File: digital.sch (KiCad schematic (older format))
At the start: 2 parts

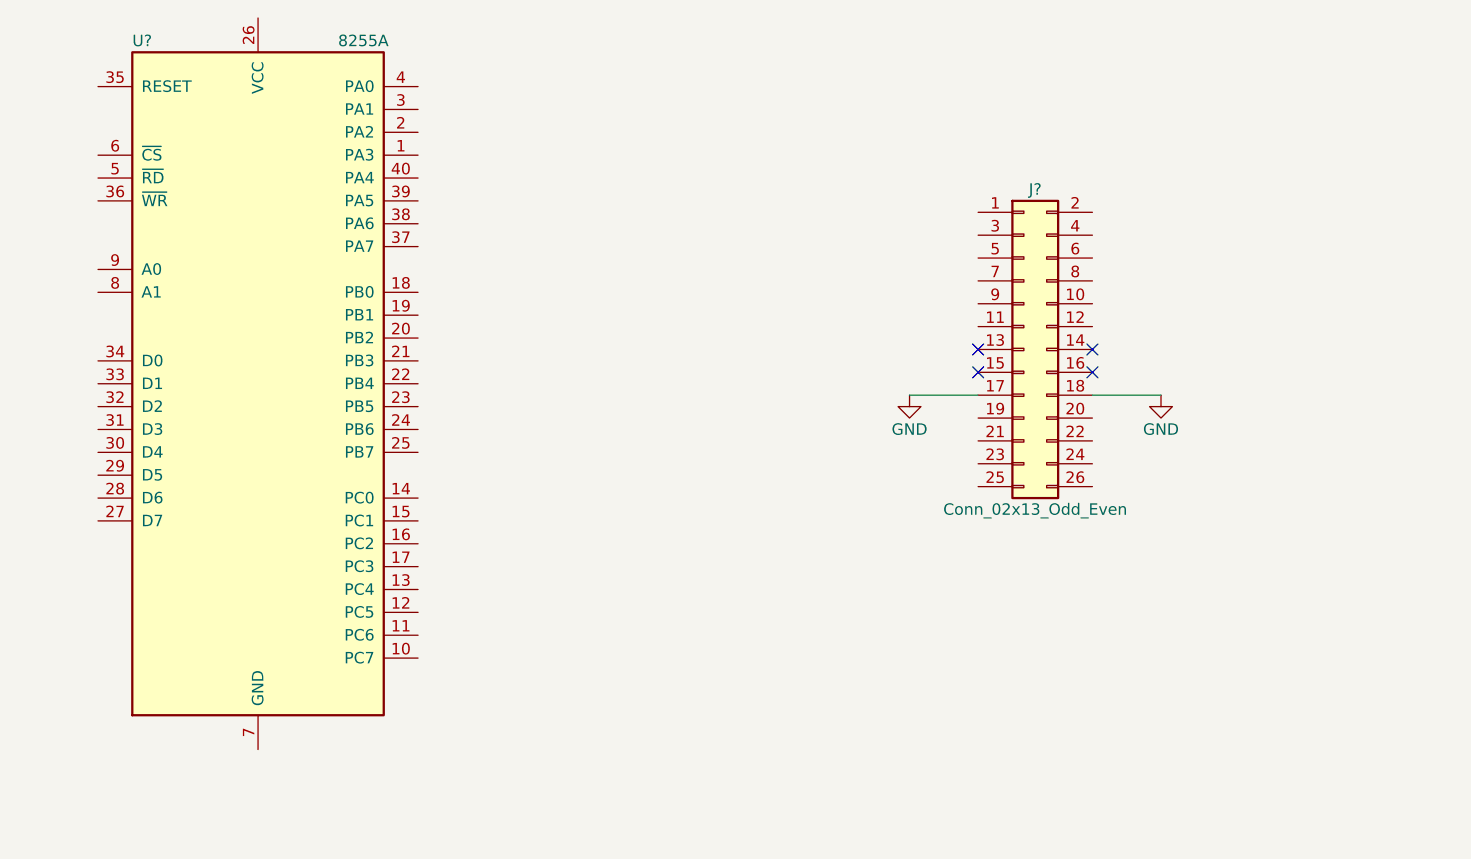
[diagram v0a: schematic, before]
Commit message: Fixed schematic to work with KiCad 5
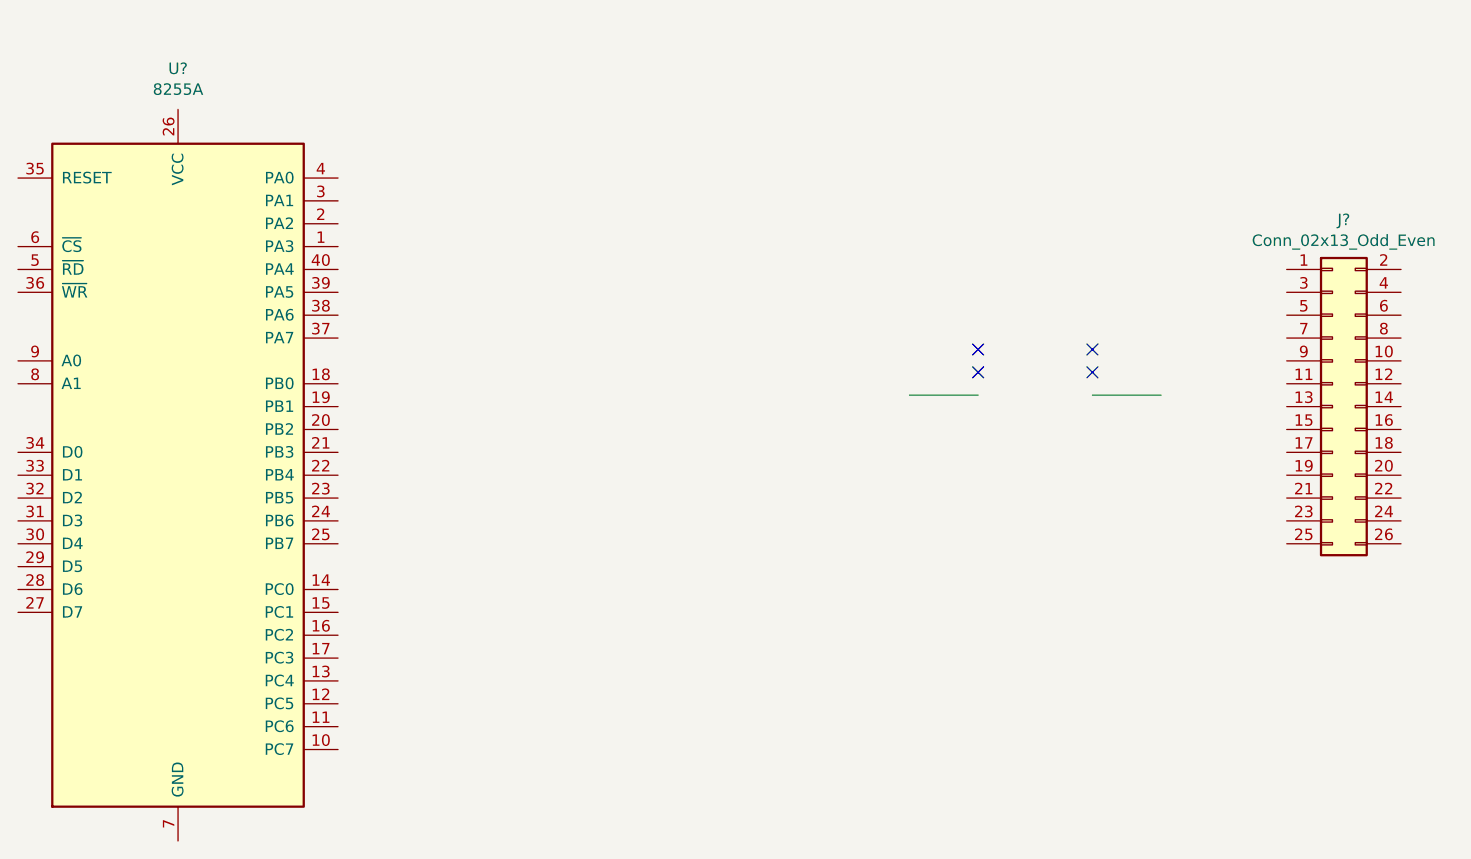
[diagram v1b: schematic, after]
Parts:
- removed J?: Conn_02x13_Odd_Even, symbol Conn_02x13_Odd_Even
- removed U?: 8255A, Housings_DIP:DIP-40_W15.24mm, symbol 8255A
- added J?: Conn_02x13_Odd_Even, symbol Connector_Generic:Conn_02x13_Odd_Even
- added U?: 8255A, Package_DIP:DIP-40_W15.24mm, symbol Interface:8255A
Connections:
- net labels removed: GND
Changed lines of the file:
@@
-EESchema Schematic File Version 2
-LIBS:power
-LIBS:device
-LIBS:switches
-LIBS:relays
-LIBS:motors
-LIBS:transistors
-LIBS:conn
-LIBS:linear
-LIBS:regul
-LIBS:74xx
-LIBS:cmos4000
-LIBS:adc-dac
-LIBS:memory
-LIBS:xilinx
-LIBS:microcontrollers
-LIBS:dsp
-LIBS:microchip
-LIBS:analog_switches
-LIBS:motorola
-LIBS:texas
-LIBS:intel
-LIBS:audio
-LIBS:interface
-LIBS:digital-audio
-LIBS:philips
-LIBS:display
-LIBS:cypress
-LIBS:siliconi
-LIBS:opto
-LIBS:atmel
-LIBS:contrib
-LIBS:valves
-EELAYER 25 0
+EESchema Schematic File Version 4
+EELAYER 26 0
 EELAYER END
 $Descr A4 11693 8268
 encoding utf-8
-Sheet 1 1
+Sheet 5 5
 Title ""
 Date ""
@@
 Comment4 ""
 $EndDescr
-$Comp
-L Conn_02x13_Odd_Even J?
-U 1 1 5B426FEC
-P 8450 3150
-F 0 "J?" H 8500 3850 50  0000 C CNN
-F 1 "Conn_02x13_Odd_Even" H 8500 2450 50  0000 C CNN
-F 2 "" H 8450 3150 50  0001 C CNN
-F 3 "" H 8450 3150 50  0001 C CNN
-	1    8450 3150
-	1    0    0    -1
-$EndComp
 NoConn ~ 8250 3250
 NoConn ~ 8250 3150
@@
 	8250 3350 7950 3350
 $Comp
-L GND #PWR?
-U 1 1 5B4270A4
-P 9050 3350
-F 0 "#PWR?" H 9050 3100 50  0001 C CNN
-F 1 "GND" H 9050 3200 50  0000 C CNN
-F 2 "" H 9050 3350 50  0001 C CNN
-F 3 "" H 9050 3350 50  0001 C CNN
-	1    9050 3350
+L Interface:8255A U?
+U 1 1 5BDEFFD9
+P 4750 3700
+F 0 "U?" H 4750 5478 50  0000 C CNN
+F 1 "8255A" H 4750 5387 50  0000 C CNN
+F 2 "Package_DIP:DIP-40_W15.24mm" H 4750 4000 50  0001 C CNN
+F 3 "http://aturing.umcs.maine.edu/~meadow/courses/cos335/Intel8255A.pdf" H 4750 4000 50  0001 C CNN
+	1    4750 3700
 	1    0    0    -1
 $EndComp
 $Comp
-L GND #PWR?
-U 1 1 5B4270BA
-P 7950 3350
-F 0 "#PWR?" H 7950 3100 50  0001 C CNN
-F 1 "GND" H 7950 3200 50  0000 C CNN
-F 2 "" H 7950 3350 50  0001 C CNN
-F 3 "" H 7950 3350 50  0001 C CNN
-	1    7950 3350
+L Connector_Generic:Conn_02x13_Odd_Even J?
+U 1 1 5BDF0194
+P 9800 3400
+F 0 "J?" H 9850 4217 50  0000 C CNN
+F 1 "Conn_02x13_Odd_Even" H 9850 4126 50  0000 C CNN
+F 2 "" H 9800 3400 50  0001 C CNN
+F 3 "~" H 9800 3400 50  0001 C CNN
+	1    9800 3400
 	1    0    0    -1
 $EndComp
-$Comp
-L 8255A U?
-U 1 1 5B4271D8
-P 5100 3300
-F 0 "U?" H 4550 4800 50  0000 L CNN
-F 1 "8255A" H 5450 4800 50  0000 L CNN
-F 2 "Housings_DIP:DIP-40_W15.24mm" H 5100 3600 50  0001 C CNN
-F 3 "" H 5100 3600 50  0001 C CNN
-	1    5100 3300
-	1    0    0    -1
-$EndComp
